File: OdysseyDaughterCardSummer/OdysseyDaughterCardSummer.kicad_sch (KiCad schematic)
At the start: 26 parts

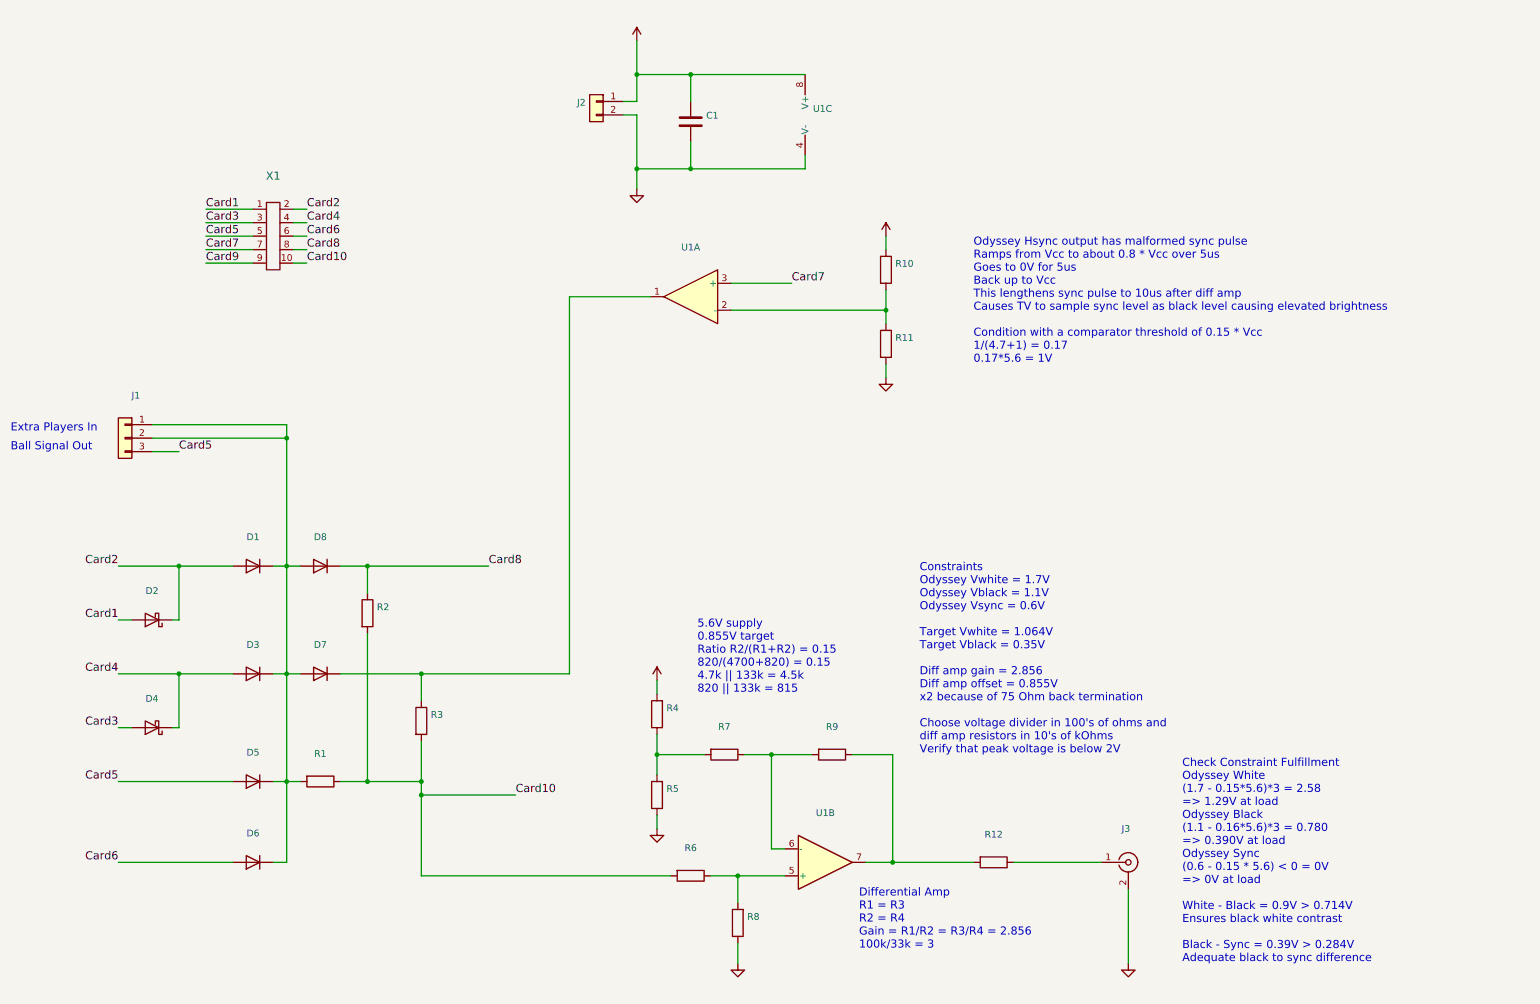
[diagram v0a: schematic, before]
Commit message: OdysseyDaughterCardSummer add logo, generate pdf, images, 3d models
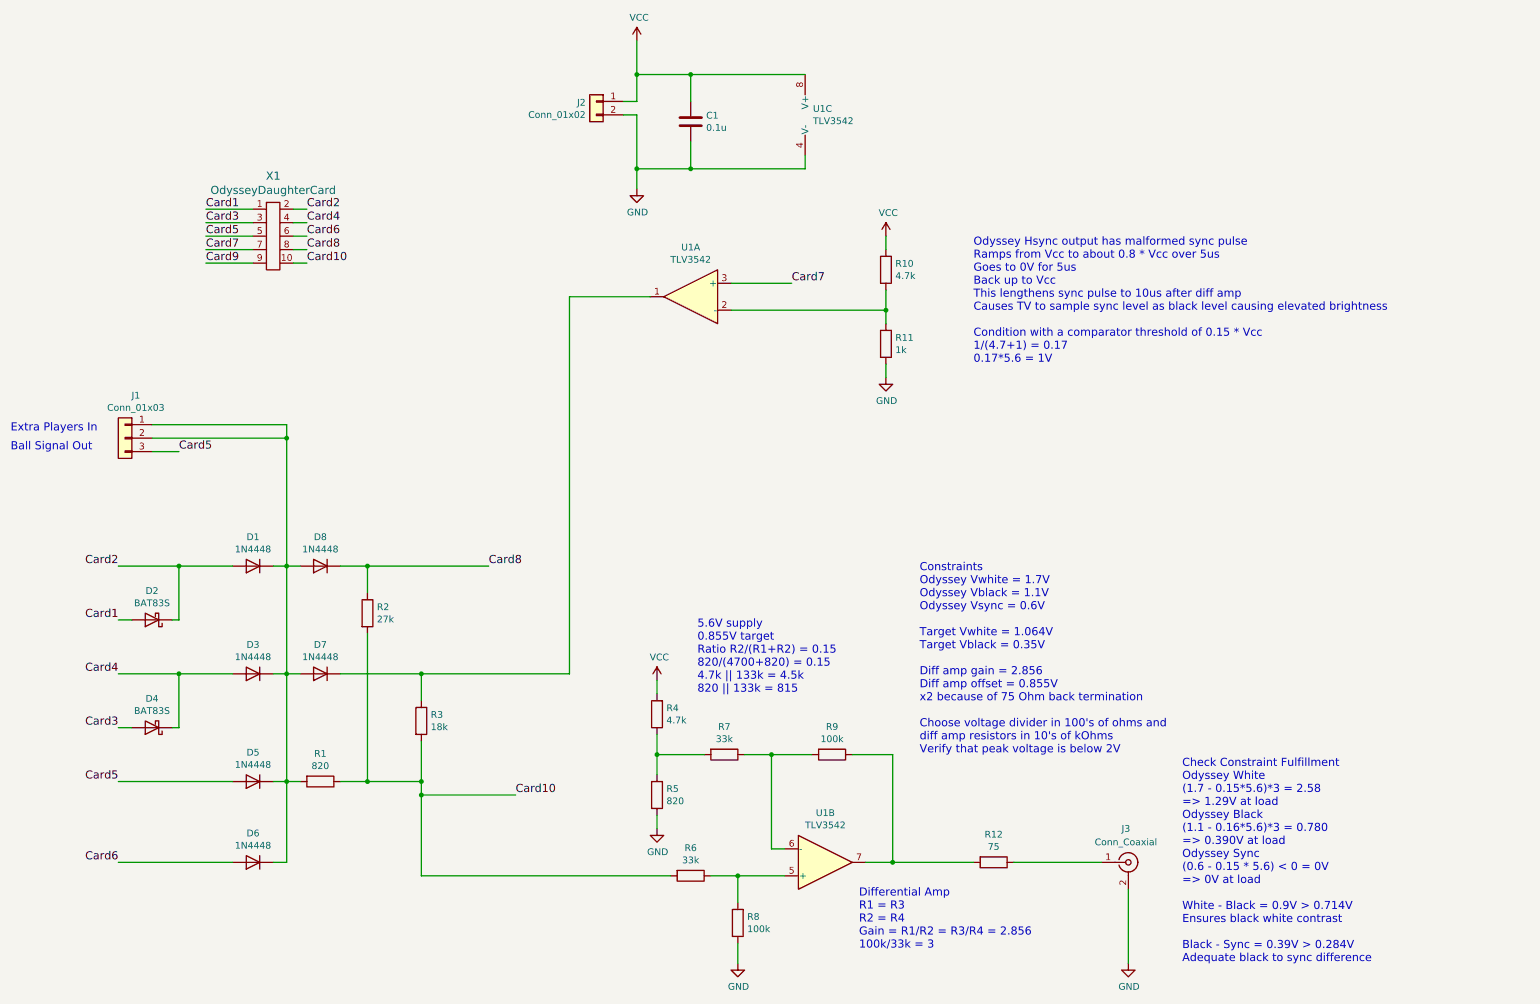
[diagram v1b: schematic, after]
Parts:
- C1: value (none) -> 0.1u; footprint (none) -> Capacitor_THT:C_Disc_D3.8mm_W2.6mm_P2.50mm
- D1, D3, D5, D6, D7, D8: value (none) -> 1N4448; footprint (none) -> Diode_THT:D_DO-35_SOD27_P7.62mm_Horizontal
- D2, D4: value (none) -> BAT83S; footprint (none) -> Diode_THT:D_DO-35_SOD27_P7.62mm_Horizontal
- J1: value (none) -> Conn_01x03; footprint (none) -> Connector_PinHeader_2.54mm:PinHeader_1x03_P2.54mm_Vertical
- J2: value (none) -> Conn_01x02; footprint (none) -> Connector_PinHeader_2.54mm:PinHeader_1x02_P2.54mm_Vertical
- J3: value (none) -> Conn_Coaxial; footprint (none) -> Connector_PinHeader_2.54mm:PinHeader_1x02_P2.54mm_Vertical
- R1, R5: value (none) -> 820; footprint (none) -> Resistor_THT:R_Axial_DIN0207_L6.3mm_D2.5mm_P7.62mm_Horizontal
- R10, R4: value (none) -> 4.7k; footprint (none) -> Resistor_THT:R_Axial_DIN0207_L6.3mm_D2.5mm_P7.62mm_Horizontal
- R11: value (none) -> 1k; footprint (none) -> Resistor_THT:R_Axial_DIN0207_L6.3mm_D2.5mm_P7.62mm_Horizontal
- R12: value (none) -> 75; footprint (none) -> Resistor_THT:R_Axial_DIN0207_L6.3mm_D2.5mm_P7.62mm_Horizontal
- R2: value (none) -> 27k; footprint (none) -> Resistor_THT:R_Axial_DIN0207_L6.3mm_D2.5mm_P7.62mm_Horizontal
- R3: value (none) -> 18k; footprint (none) -> Resistor_THT:R_Axial_DIN0207_L6.3mm_D2.5mm_P7.62mm_Horizontal
- R6, R7: value (none) -> 33k; footprint (none) -> Resistor_THT:R_Axial_DIN0207_L6.3mm_D2.5mm_P7.62mm_Horizontal
- R8, R9: value (none) -> 100k; footprint (none) -> Resistor_THT:R_Axial_DIN0207_L6.3mm_D2.5mm_P7.62mm_Horizontal
- U1: value (none) -> TLV3542; footprint (none) -> Package_SO:SOIC-8_3.9x4.9mm_P1.27mm
- X1: value (none) -> OdysseyDaughterCard; footprint (none) -> Odyssey_Daughter_Card:Odyssey_Daughter_Card
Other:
- company: University of Pittsburgh - Odyssey Restoration Project -> University of Pittsburgh - OdysseyNow
